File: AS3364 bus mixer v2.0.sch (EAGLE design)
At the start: 64 parts, among them IC1 TL072JT, IC2 TL072JT, IC3 TL072JT, IC30 TL072JT, IC4 TL072JT, IC5 79L09F, IC6 78L09F, IC7 CH446Q

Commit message: Working on v2.0
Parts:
- added R37, R38, R39, R40, R41, R42, R43, R44: 36k, rcl:R-EU_R0402
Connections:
- net SW1 renamed SW1A
- removed net BITCRUSH_IN: IC7.Y5, SV1.13
- removed net DIST_IN: IC7.Y4, SV1.14
- removed net SW2: IC7.X1, R15.2
- removed net SW3: IC7.X2, R17.2
- removed net SW4: IC7.X3, R14.2
- removed net SW5: IC7.X4, R33.2
- removed net SW6: IC7.X5, R32.2
- removed net SW7: IC7.X6, R34.2
- removed net SW8: IC7.X7, R31.2
- new net SW1B: IC7.X1, R40.2
- new net SW2A: IC7.X2, R15.2
- new net SW2B: IC7.X3, R37.2
- new net SW3A: IC7.X4, R17.2
- new net SW3B: IC7.X5
- new net SW4A: IC7.X6, R14.2
- new net SW4B: IC7.X7, R38.2, R39.2
- new net SW5A: IC7.X8, R33.2
- new net SW5B: IC7.X9, R44.2
- new net SW6A: IC7.X10, R32.2
- new net SW6B: IC7.X11, R41.2
- new net SW7A: IC7.X12, R34.2
- new net SW7B: IC7.X13, R43.2
- new net SW8A: IC7.X14, R31.2
- new net SW8B: IC7.X15, R42.2
- net OUT1: now also R40.1
- net OUT2: now also R37.1
- net OUT3: now also R39.1
- net OUT4: now also R38.1
- net OUT5: now also R44.1
- net OUT6: now also R41.1
- net OUT7: now also R43.1
- net OUT8: now also R42.1
- net SUM_A: no longer IC7.X8
- net SUM_B: no longer IC7.X9
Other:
- note removed: "V1.0 of this circuit has two shortcomings: - an input may only go to a single output - the sum of the waves may only reach approx 8V or the input on SUM A/B will clip"

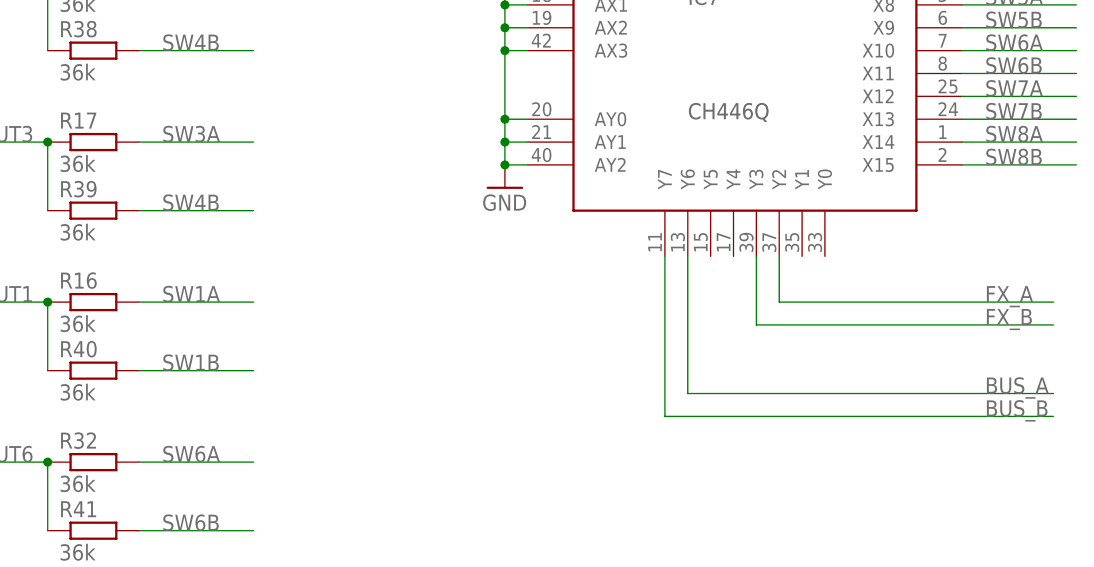
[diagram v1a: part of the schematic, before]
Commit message: Finished tracing v2.0 of bus mixer
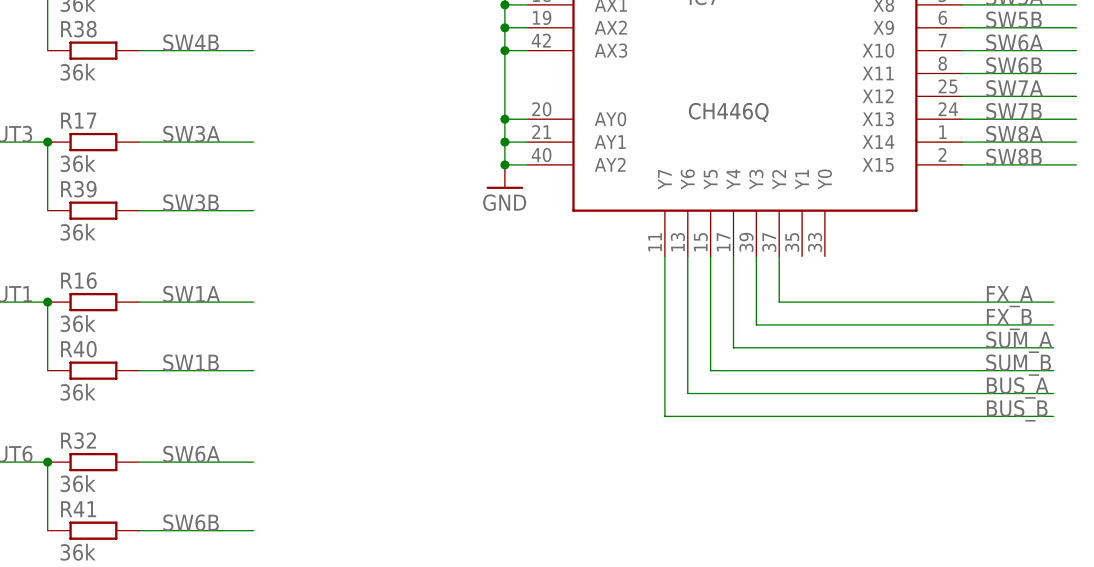
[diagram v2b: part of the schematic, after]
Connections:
- net SUM_A: now also IC7.Y4
- net SUM_B: now also IC7.Y5
- net SW3B: now also R39.2
- net SW4B: no longer R39.2
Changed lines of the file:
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@@
 <wire x1="218.44" y1="-43.18" x2="233.68" y2="-43.18" width="0.1524" layer="91"/>
+</segment>
+<segment>
+<pinref part="IC7" gate="G$1" pin="Y4"/>
+<wire x1="203.2" y1="33.02" x2="203.2" y2="22.86" width="0.1524" layer="91"/>
+<wire x1="203.2" y1="22.86" x2="238.76" y2="22.86" width="0.1524" layer="91"/>
+<label x="231.14" y="22.86" size="1.778" layer="95"/>
 </segment>
 </net>
@@
 <wire x1="218.44" y1="-63.5" x2="233.68" y2="-63.5" width="0.1524" layer="91"/>
 </segment>
+<segment>
+<pinref part="IC7" gate="G$1" pin="Y5"/>
+<wire x1="200.66" y1="33.02" x2="200.66" y2="20.32" width="0.1524" layer="91"/>
+<wire x1="200.66" y1="20.32" x2="238.76" y2="20.32" width="0.1524" layer="91"/>
+<label x="231.14" y="20.32" size="1.778" layer="95"/>
+</segment>
 </net>
 <net name="FX_A" class="0">
@@
 <label x="231.14" y="68.58" size="1.778" layer="95"/>
 </segment>
+<segment>
+<pinref part="R39" gate="G$1" pin="2"/>
+<wire x1="149.86" y1="38.1" x2="137.16" y2="38.1" width="0.1524" layer="91"/>
+<label x="139.7" y="38.1" size="1.778" layer="95"/>
+</segment>
 </net>
 <net name="SW4A" class="0">
@@
 <label x="139.7" y="55.88" size="1.778" layer="95"/>
 </segment>
-<segment>
-<pinref part="R39" gate="G$1" pin="2"/>
-<wire x1="149.86" y1="38.1" x2="137.16" y2="38.1" width="0.1524" layer="91"/>
-<label x="139.7" y="38.1" size="1.778" layer="95"/>
-</segment>
-</net>
+</net>

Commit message: Ordered 10 bus mixer v2.0
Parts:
- removed C16: 100nF, rcl:C-EUC0402
- added C8: 100nF, rcl:C-EUC0402
- C1, C5: value 5nF -> 100nF
- C10, C11: value 100nF -> 5nF
- C12: value 100nF -> 0.33uF; device rcl:C-EUC0402 -> resistor:C-EUC0603
- C15: value 0.33uF -> 100nF; device resistor:C-EUC0603 -> rcl:C-EUC0402
- IC1: value TL072JT -> 78L09F; device joakim:TL072JT -> linear:78L09F
- IC2: value TL072JT -> 79L09F; device joakim:TL072JT -> joakim:79L09F
- IC5: value 79L09F -> TL072JT; device joakim:79L09F -> joakim:TL072JT
- IC6: value 78L09F -> TL072JT; device linear:78L09F -> joakim:TL072JT
- R11, R26, R27, R28, R29, R9: value 22k -> 33k
- R13, R30: value 100R -> 33k
- R14, R16, R6, R8: value 36k -> 22k
- R15, R22, R23, R24, R25, R31, R32, R33, R34, R37, R38, R39, R40, R41, R42, R5, R7: value 36k -> 33k
- R17: value 36k -> 100R
- R18: value 33k -> 100R
- R2, R4: value 33k -> 22k
- R35, R36: value 220k -> 33k
- R43, R44: value 36k -> 220k
- renumbered C17 to C14, DA1 to IC10, DA2 to IC9, IC30 to IC8, R47 to R45, R48 to R46, SV1 to X1
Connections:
- net +12V: now also C1.2, C5.2, C7.2, C8.2, C9.2, IC1.VI, IC5P.V+, IC6P.V+; no longer C10.2, C11.2, C13.2, C2.2, C4.2, IC1P.V+, IC2P.V+, IC6.VI
- net +9V: now also IC1.VO; no longer IC6.VO
- net -12V: now also C13.1, C5.1, C6.1, C8.1, IC2.VI, IC5P.V-, IC6P.V-; no longer C11.1, C12.1, C15.1, C3.1, IC1P.V-, IC2P.V-, IC5.VI
- net -9V: now also C15.2, IC2.VO; no longer C16.2, IC5.VO
- net BUS_A: now also R43.2; no longer R35.2
- net BUS_B: now also R44.2; no longer R36.2
- net CON1: now also IC4A.+IN, R22.2; no longer IC1A.+IN, R6.2
- net CON2: now also IC4B.+IN, R19.2; no longer IC1B.+IN, R7.2
- net CON3: now also IC3A.+IN, R21.2; no longer IC2A.+IN, R5.2
- net CON4: now also IC3B.+IN, R20.2; no longer IC2B.+IN, R8.2
- net CON5: now also IC6A.+IN, R26.2; no longer IC3A.+IN, R23.2
- net CON6: now also IC6B.+IN, R23.2; no longer IC3B.+IN, R24.2
- net CON7: now also IC5A.+IN, R25.2; no longer IC4A.+IN, R22.2
- net CON8: now also IC5B.+IN, R24.2; no longer IC4B.+IN, R25.2
- net CV1: now also R7.1; no longer R2.1
- net CV2: now also R1.1; no longer R3.1
- net CV2_IN: now also R1.2, R2.2; no longer R11.2, R3.2
- net CV3: now also R5.1; no longer R1.1
- net CV4: now also R3.1; no longer R4.1
- net CV5: now also R15.1; no longer R19.1
- net CV6: now also R9.1; no longer R20.1
- net CV6_IN: now also R10.2, R9.2; no longer R20.2, R28.2
- net CV7: now also R13.1; no longer R18.1
- net CV8: now also R11.1; no longer R21.1
- net GND: now also C11.1, C12.1, C13.2, C15.1, C2.2, C3.1, C4.2, IC1.GND, IC1.GND@1, IC2.GND, R14.1, R16.1, R19.1, R2.1, R20.1, R21.1, R4.1, R43.1, R44.1; no longer C13.1, C15.2, C16.1, C5.1, C6.1, C7.2, C9.2, IC5.GND, IC6.GND, IC6.GND@1, R11.1, R27.1, R28.1, R29.1, R35.1, R36.1, R5.1, R7.1, R9.1
- net N$1: now also R18.2; no longer R30.2
- net N$10: now also R3.2; no longer R12.2
- net N$12: now also R5.2, R6.2; no longer R1.2, R9.2
- net N$14: now also C10.2, R17.1; no longer C5.2, R13.1
- net N$2: now also R17.2; no longer R13.2
- net N$21: now also R7.2, R8.2; no longer R10.2, R2.2
- net N$3: now also R11.2, R12.2; no longer R21.2, R29.2
- net N$5: now also R13.2, R14.2; no longer R18.2, R26.2
- net N$7: now also R15.2, R16.2; no longer R19.2, R27.2
- net N$8: now also C11.2, R18.1; no longer C1.2, R30.1
- net OUT1: now also IC4A.-IN, IC4A.OUT, R33.1, R34.1; no longer IC1A.-IN, IC1A.OUT, R16.1, R40.1
- net OUT2: now also IC4B.-IN, IC4B.OUT, R27.1, R28.1; no longer IC1B.-IN, IC1B.OUT, R15.1, R37.1
- net OUT3: now also IC3A.-IN, IC3A.OUT, R31.1, R32.1; no longer IC2A.-IN, IC2A.OUT, R17.1, R39.1
- net OUT4: now also IC3B.-IN, IC3B.OUT, R29.1, R30.1; no longer IC2B.-IN, IC2B.OUT, R14.1, R38.1
- net OUT5: now also IC6A.-IN, IC6A.OUT, R41.1, R42.1; no longer IC3A.-IN, IC3A.OUT, R33.1, R44.1
- net OUT6: now also IC6B.-IN, IC6B.OUT, R35.1, R36.1; no longer IC3B.-IN, IC3B.OUT, R32.1, R41.1
- net OUT7: now also IC5A.-IN, IC5A.OUT, R39.1, R40.1; no longer IC4A.-IN, IC4A.OUT, R34.1, R43.1
- net OUT8: now also IC5B.-IN, IC5B.OUT, R37.1, R38.1; no longer IC4B.-IN, IC4B.OUT, R31.1, R42.1
- net SW1A: now also R33.2; no longer R16.2
- net SW1B: now also R34.2; no longer R40.2
- net SW2A: now also R27.2; no longer R15.2
- net SW2B: now also R28.2; no longer R37.2
- net SW3A: now also R31.2; no longer R17.2
- net SW3B: now also R32.2; no longer R39.2
- net SW4A: now also R29.2; no longer R14.2
- net SW4B: now also R30.2; no longer R38.2
- net SW5A: now also R41.2; no longer R33.2
- net SW5B: now also R42.2; no longer R44.2
- net SW6A: now also R35.2; no longer R32.2
- net SW6B: now also R36.2; no longer R41.2
- net SW7A: now also R39.2; no longer R34.2
- net SW7B: now also R40.2; no longer R43.2
- net SW8A: now also R37.2; no longer R31.2
- net SW8B: now also R38.2; no longer R42.2
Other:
- moved on the sheet: C1, C10, C11, C12, C13, C15, C2, C3, C4, C5, C6, C7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
